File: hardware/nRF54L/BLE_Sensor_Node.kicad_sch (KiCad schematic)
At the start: 42 parts, among them U1 nRF54L05-QFXX, U2 SHTC3, U3 HDC2010, X1 32M, X2 32.768k

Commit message: nRF schematics rev: A
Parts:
- C1: footprint (none) -> Capacitor_SMD:C_0603_1608Metric; AX (none) -> 27204
- C10, C5: DigiKey (none) -> 490-12731-1-ND
- C11: DigiKey (none) -> 490-17132-1-ND
- C12, C13: DigiKey (none) -> 490-3194-1-ND
- C16: footprint (none) -> Capacitor_SMD:C_0805_2012Metric
- C7: DigiKey (none) -> 712-QLCD250Q1R5B1GV001TCT-ND
- C9: DigiKey (none) -> 490-11205-1-ND
- FB1: footprint (none) -> Inductor_SMD:L_0603_1608Metric; AX (none) -> 73236
- L1: DigiKey (none) -> 490-12065-1-ND
- L2: DigiKey (none) -> 490-15398-1-ND
- L3, L4: DigiKey (none) -> 490-15430-1-ND
- L5: value L -> 7.3n; DigiKey (none) -> 490-6844-1-ND
- L6: value L -> 6.7n; DigiKey (none) -> 490-LQW15AN6N7B00DCT-ND
- L7: now not fitted; now left out of the parts list
- R1: AX (none) -> 201001
- R2, R3: AX (none) -> 204701
- X1: value 32M -> 32MHz
- X2: value 32.768k -> 32.768kHz
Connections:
- net ANT: now also AE1.1 (Feed), L6.2, L7.1; no longer C11.1, L4.2, L5.2, L6.1
- net XL1: now reaches U1.1 (P1.00), X2.2
- net XL2: now reaches U1.2 (P1.01), X2.1
- net XC1: now reaches U1.34 (XC1), X1.1
- net XC2: now reaches U1.35 (XC2), X1.3
- new net: C11.1, L4.2, L5.2, L6.1
- no-connect marks 0 -> 26
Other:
- title: BLE Sensor Node (nRF54L varian) -> BLE Sensor Node (nRF54L variant)
- moved on the sheet: AE1, L1, X1, X2

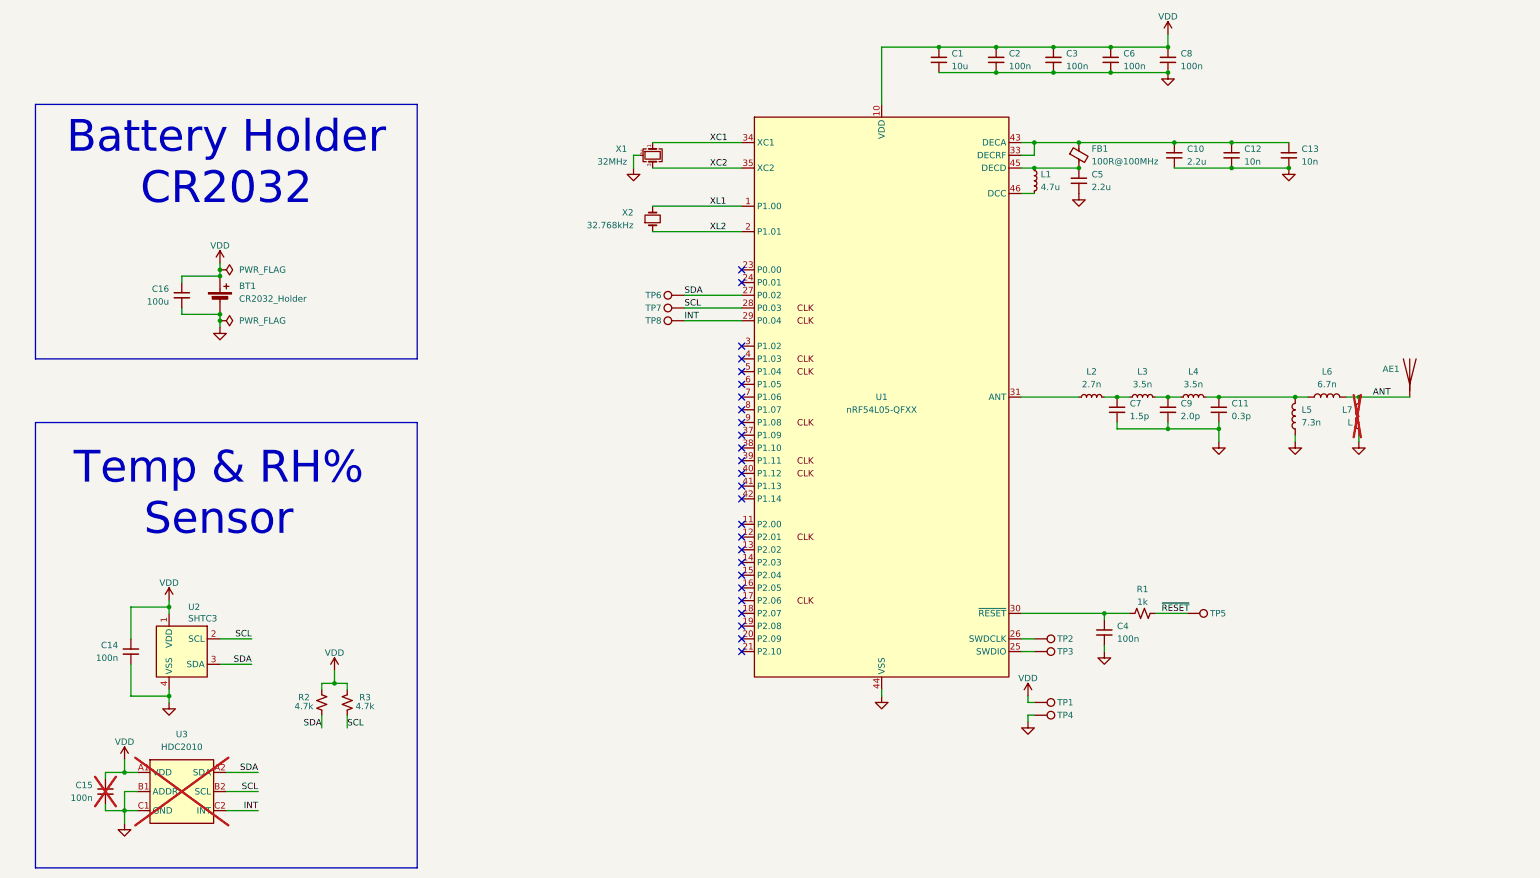
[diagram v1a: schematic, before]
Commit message: nRF54 variant routing
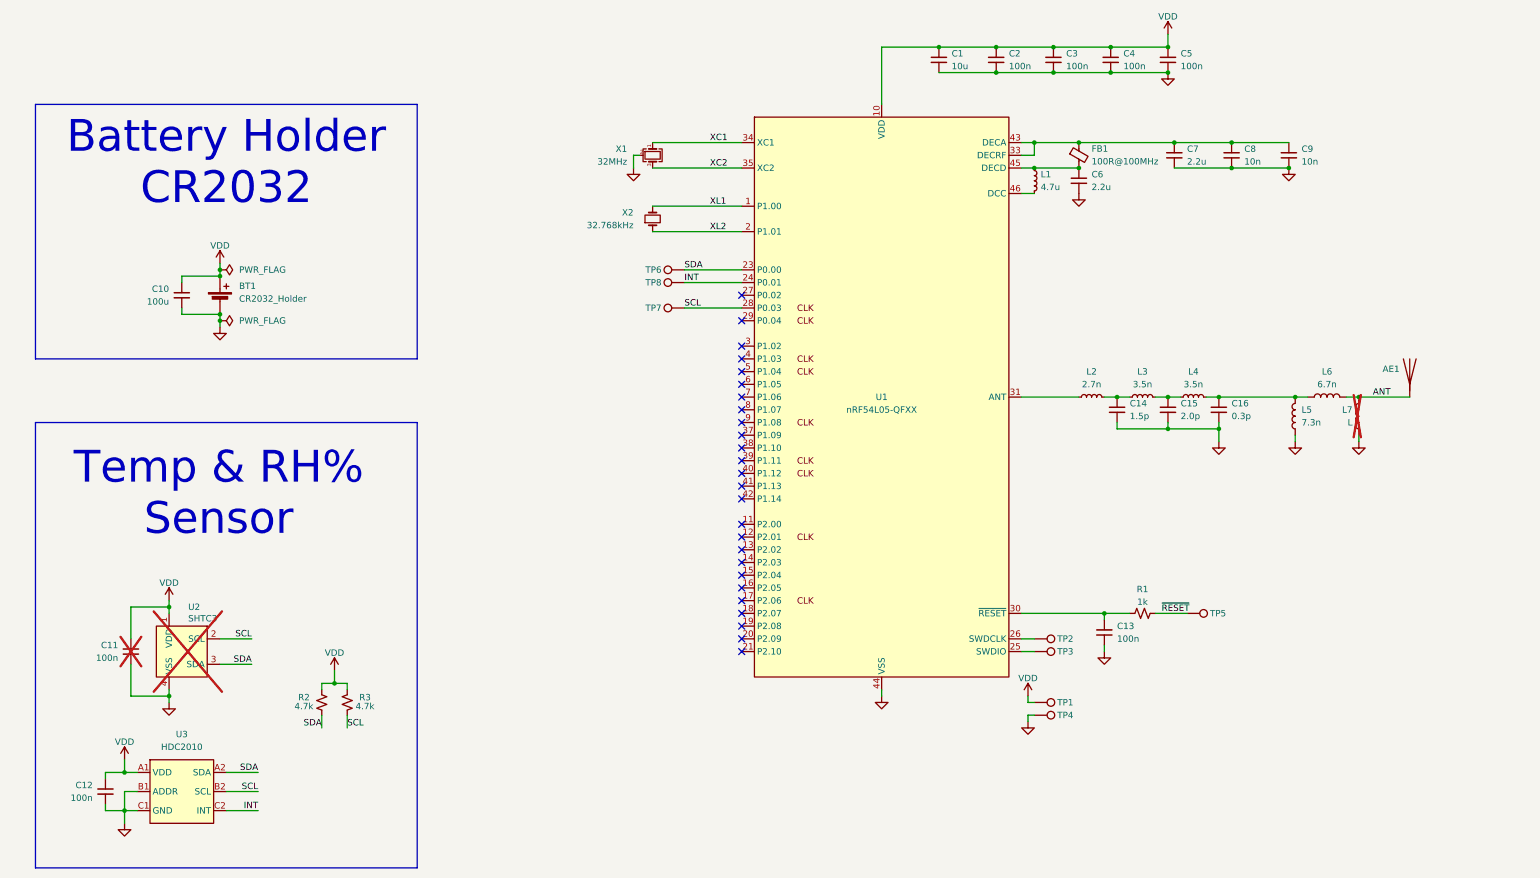
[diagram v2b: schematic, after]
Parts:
- C11: renamed from C14; now not fitted; now left out of the parts list
- C12: renamed from C15; now fitted; now in the parts list
- TP1, TP2, TP3, TP4: footprint TestPoint:TestPoint_Pad_D1.0mm -> TestPoint:TestPoint_Pad_D1.5mm
- U1: footprint Package_DFN_QFN:QFN-48-1EP_6x6mm_P0.4mm_EP4.6x4.6mm_ThermalVias -> BLE_Sensor_Node:VQFN-48-1EP_6x6mm_P0.4mm_EP4.1x4.1mm_ThermalVias
- U2: now not fitted; now left out of the parts list
- U3: now fitted; now in the parts list
- renumbered C16 to C10, C4 to C13, C7 to C14, C9 to C15, C11 to C16, C6 to C4, C8 to C5, C5 to C6, C10 to C7, C12 to C8, C13 to C9
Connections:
- net INT: now also U1.24 (P0.01); no longer U1.29 (P0.04)
- net SDA: now also U1.23 (P0.00); no longer U1.27 (P0.02)
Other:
- moved on the sheet: TP6, TP8
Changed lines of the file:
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@@
 	)
 	(no_connect
+		(at 179.07 132.08)
+	)
+	(no_connect
 		(at 179.07 165.1)
 	)
@@
 	)
 	(no_connect
-		(at 179.07 124.46)
-	)
-	(no_connect
 		(at 179.07 144.78)
 	)
@@
 	)
 	(no_connect
-		(at 179.07 121.92)
+		(at 179.07 190.5)
 	)
 	(no_connect
-		(at 179.07 190.5)
+		(at 179.07 127)
 	)
 	(no_connect
@@
 	(wire
 		(pts
-			(xy 167.64 127) (xy 179.07 127)
+			(xy 167.64 121.92) (xy 179.07 121.92)
 		)
 		(stroke
@@
 	(wire
 		(pts
-			(xy 167.64 132.08) (xy 179.07 132.08)
+			(xy 167.64 124.46) (xy 179.07 124.46)
 		)
 		(stroke
@@
 	)
 	(label "INT"
-		(at 167.64 132.08 0)
+		(at 167.64 124.46 0)
 		(effects
 			(font
@@
 	)
 	(label "SDA"
-		(at 167.64 127 0)
+		(at 167.64 121.92 0)
 		(effects
 			(font
@@
 		(dnp no)
 		(fields_autoplaced yes)
-		(property "Reference" "C10"
-			(at 267.97 97.7962 0)
+		(property "Reference" "C7"
+			(at 267.97 97.7899 0)
 			(show_name no)
 			(do_not_autoplace no)
@@
 		)
 		(property "Value" "2.2u"
-			(at 267.97 100.3362 0)
+			(at 267.97 100.3299 0)
 			(show_name no)
 			(do_not_autoplace no)
@@
 			(project "BLE_Sensor_Node"
 				(path "/3be841bb-f0fa-4f59-8a52-40b0b50ca4ae"
-					(reference "C10")
+					(reference "C7")
 					(unit 1)
 				)
@@
 		(dnp no)
 		(fields_autoplaced yes)
-		(property "Reference" "C5"
-			(at 248.92 102.8762 0)
+		(property "Reference" "C6"
+			(at 248.92 102.8699 0)
 			(show_name no)
 			(do_not_autoplace no)
@@
 		)
 		(property "Value" "2.2u"
-			(at 248.92 105.4162 0)
+			(at 248.92 105.4099 0)
 			(show_name no)
 			(do_not_autoplace no)
@@
 			(project "BLE_Sensor_Node"
 				(path "/3be841bb-f0fa-4f59-8a52-40b0b50ca4ae"
-					(reference "C5")
+					(reference "C6")
 					(unit 1)
 				)
@@
 		(dnp no)
 		(fields_autoplaced yes)
-		(property "Reference" "C11"
-			(at 276.86 148.5962 0)
+		(property "Reference" "C16"
+			(at 276.86 148.5899 0)
 			(show_name no)
 			(do_not_autoplace no)
@@
 		)
 		(property "Value" "0.3p"
-			(at 276.86 151.1362 0)
+			(at 276.86 151.1299 0)
 			(show_name no)
 			(do_not_autoplace no)
@@
 			(project "BLE_Sensor_Node"
 				(path "/3be841bb-f0fa-4f59-8a52-40b0b50ca4ae"
-					(reference "C11")
+					(reference "C16")
 					(unit 1)
 				)
@@
 		(body_style 1)
 		(exclude_from_sim no)
-		(in_bom no)
+		(in_bom yes)
 		(on_board yes)
 		(in_pos_files yes)
-		(dnp yes)
+		(dnp no)
 		(fields_autoplaced yes)
 		(property "Reference" "U3"
@@
 			)
 		)
-		(property "Footprint" "Package_DFN_QFN:QFN-48-1EP_6x6mm_P0.4mm_EP4.6x4.6mm_ThermalVias"
+		(property "Footprint" "BLE_Sensor_Node:VQFN-48-1EP_6x6mm_P0.4mm_EP4.1x4.1mm_ThermalVias"
 			(at 207.01 220.98 0)
 			(hide yes)
@@
 		(dnp no)
 		(fields_autoplaced yes)
-		(property "Reference" "C7"
-			(at 256.54 148.5962 0)
+		(property "Reference" "C14"
+			(at 256.54 148.5899 0)
 			(show_name no)
 			(do_not_autoplace no)
@@
 		)
 		(property "Value" "1.5p"
-			(at 256.54 151.1362 0)
+			(at 256.54 151.1299 0)
 			(show_name no)
 			(do_not_autoplace no)
@@
 			(project "BLE_Sensor_Node"
 				(path "/3be841bb-f0fa-4f59-8a52-40b0b50ca4ae"
-					(reference "C7")
+					(reference "C14")
 					(unit 1)
 				)
@@
 		(body_style 1)
 		(exclude_from_sim no)
-		(in_bom yes)
+		(in_bom no)
 		(on_board yes)
 		(in_pos_files yes)
-		(dnp no)
-		(property "Reference" "C14"
+		(dnp yes)
+		(property "Reference" "C11"
 			(at 54.61 196.8562 0)
 			(show_name no)
@@
 			(project "BLE_Sensor_Node"
 				(path "/3be841bb-f0fa-4f59-8a52-40b0b50ca4ae"
-					(reference "C14")
+					(reference "C11")
 					(unit 1)
 				)
@@
 			)
 		)
-		(property "Footprint" "TestPoint:TestPoint_Pad_D1.0mm"
+		(property "Footprint" "TestPoint:TestPoint_Pad_D1.5mm"
 			(at 237.49 215.9 0)
 			(hide yes)
@@
 		(dnp no)
 		(fields_autoplaced yes)
-		(property "Reference" "C12"
-			(at 279.4 97.7962 0)
+		(property "Reference" "C8"
+			(at 279.4 97.7899 0)
 			(show_name no)
 			(do_not_autoplace no)
@@
 		)
 		(property "Value" "10n"
-			(at 279.4 100.3362 0)
+			(at 279.4 100.3299 0)
 			(show_name no)
 			(do_not_autoplace no)
@@
 			(project "BLE_Sensor_Node"
 				(path "/3be841bb-f0fa-4f59-8a52-40b0b50ca4ae"
-					(reference "C12")
+					(reference "C8")
 					(unit 1)
 				)
@@
 			)
 		)
-		(property "Footprint" "TestPoint:TestPoint_Pad_D1.0mm"
+		(property "Footprint" "TestPoint:TestPoint_Pad_D1.5mm"
 			(at 237.49 200.66 0)
 			(hide yes)
@@
 		(dnp no)
 		(fields_autoplaced yes)
-		(property "Reference" "C9"
-			(at 266.7 148.5962 0)
+		(property "Reference" "C15"
+			(at 266.7 148.5899 0)
 			(show_name no)
 			(do_not_autoplace no)
@@
 		)
 		(property "Value" "2.0p"
-			(at 266.7 151.1362 0)
+			(at 266.7 151.1299 0)
 			(show_name no)
 			(do_not_autoplace no)
@@
 			(project "BLE_Sensor_Node"
 				(path "/3be841bb-f0fa-4f59-8a52-40b0b50ca4ae"
-					(reference "C9")
+					(reference "C15")
 					(unit 1)
 				)
@@
 	(symbol
 		(lib_id "Connector:TestPoint")
-		(at 167.64 127 90)
+		(at 167.64 121.92 90)
 		(unit 1)
 		(body_style 1)
@@
 		(dnp no)
 		(property "Reference" "TP6"
-			(at 163.068 127 90)
+			(at 163.068 121.92 90)
 			(show_name no)
 			(do_not_autoplace no)
@@
 		)
 		(property "Value" "TestPoint"
-			(at 162.56 125.7301 90)
+			(at 162.56 120.6501 90)
 			(hide yes)
 			(show_name no)
@@
 		)
 		(property "Footprint" "TestPoint:TestPoint_Pad_D1.0mm"
-			(at 167.64 121.92 0)
+			(at 167.64 116.84 0)
 			(hide yes)
 			(show_name no)
@@
 		)
 		(property "Datasheet" ""
-			(at 167.64 121.92 0)
+			(at 167.64 116.84 0)
 			(hide yes)
 			(show_name no)
@@
 		)
 		(property "Description" "test point"
-			(at 167.64 127 0)
+			(at 167.64 121.92 0)
 			(hide yes)
 			(show_name no)
@@
 		(dnp no)
 		(fields_autoplaced yes)
-		(property "Reference" "C8"
-			(at 266.7 78.7462 0)
+		(property "Reference" "C5"
+			(at 266.7 78.7399 0)
 			(show_name no)
 			(do_not_autoplace no)
@@
 		)
 		(property "Value" "100n"
-			(at 266.7 81.2862 0)
+			(at 266.7 81.2799 0)
 			(show_name no)
 			(do_not_autoplace no)
@@
 			(project "BLE_Sensor_Node"
 				(path "/3be841bb-f0fa-4f59-8a52-40b0b50ca4ae"
-					(reference "C8")
+					(reference "C5")
 					(unit 1)
 				)
@@
 		(body_style 1)
 		(exclude_from_sim no)
-		(in_bom no)
+		(in_bom yes)
 		(on_board yes)
 		(in_pos_files yes)
-		(dnp yes)
-		(property "Reference" "C15"
+		(dnp no)
+		(property "Reference" "C12"
 			(at 49.53 224.7962 0)
 			(show_name no)
@@
 			(project "BLE_Sensor_Node"
 				(path "/3be841bb-f0fa-4f59-8a52-40b0b50ca4ae"
-					(reference "C15")
+					(reference "C12")
 					(unit 1)
 				)
@@
 			)
 		)
-		(property "Footprint" "TestPoint:TestPoint_Pad_D1.0mm"
+		(property "Footprint" "TestPoint:TestPoint_Pad_D1.5mm"
 			(at 237.49 213.36 0)
 			(hide yes)
@@
 		(body_style 1)
 		(exclude_from_sim no)
-		(in_bom yes)
+		(in_bom no)
 		(on_board yes)
 		(in_pos_files yes)
-		(dnp no)
+		(dnp yes)
 		(property "Reference" "U2"
 			(at 68.58 189.23 0)
@@
 		(dnp no)
 		(fields_autoplaced yes)
-		(property "Reference" "C4"
-			(at 254 193.0462 0)
+		(property "Reference" "C13"
+			(at 254 193.0399 0)
 			(show_name no)
 			(do_not_autoplace no)
@@
 		)
 		(property "Value" "100n"
-			(at 254 195.5862 0)
+			(at 254 195.5799 0)
 			(show_name no)
 			(do_not_autoplace no)
@@
 			(project "BLE_Sensor_Node"
 				(path "/3be841bb-f0fa-4f59-8a52-40b0b50ca4ae"
-					(reference "C4")
+					(reference "C13")
 					(unit 1)
 				)
@@
 	(symbol
 		(lib_id "Connector:TestPoint")
-		(at 167.64 132.08 90)
+		(at 167.64 124.46 90)
 		(unit 1)
 		(body_style 1)
@@
 		(dnp no)
 		(property "Reference" "TP8"
-			(at 163.068 132.08 90)
+			(at 163.068 124.46 90)
 			(show_name no)
 			(do_not_autoplace no)
@@
 		)
 		(property "Value" "TestPoint"
-			(at 162.56 130.8101 90)
+			(at 162.56 123.1901 90)
 			(hide yes)
 			(show_name no)
@@
 		)
 		(property "Footprint" "TestPoint:TestPoint_Pad_D1.0mm"
-			(at 167.64 127 0)
+			(at 167.64 119.38 0)
 			(hide yes)
 			(show_name no)
@@
 		)
 		(property "Datasheet" ""
-			(at 167.64 127 0)
+			(at 167.64 119.38 0)
 			(hide yes)
 			(show_name no)
@@
 		)
 		(property "Description" "test point"
-			(at 167.64 132.08 0)
+			(at 167.64 124.46 0)
 			(hide yes)
 			(show_name no)
@@
 		(dnp no)
 		(fields_autoplaced yes)
-		(property "Reference" "C13"
-			(at 290.83 97.7962 0)
+		(property "Reference" "C9"
+			(at 290.83 97.7899 0)
 			(show_name no)
 			(do_not_autoplace no)
@@
 		)
 		(property "Value" "10n"
-			(at 290.83 100.3362 0)
+			(at 290.83 100.3299 0)
 			(show_name no)
 			(do_not_autoplace no)
@@
 			(project "BLE_Sensor_Node"
 				(path "/3be841bb-f0fa-4f59-8a52-40b0b50ca4ae"
-					(reference "C13")
+					(reference "C9")
 					(unit 1)
 				)
@@
 			)
 		)
-		(property "Footprint" "TestPoint:TestPoint_Pad_D1.0mm"
+		(property "Footprint" "TestPoint:TestPoint_Pad_D1.5mm"
 			(at 237.49 203.2 0)
 			(hide yes)
@@
 		(dnp no)
 		(fields_autoplaced yes)
-		(property "Reference" "C6"
-			(at 255.27 78.7462 0)
+		(property "Reference" "C4"
+			(at 255.27 78.7399 0)
 			(show_name no)
 			(do_not_autoplace no)
@@
 		)
 		(property "Value" "100n"
-			(at 255.27 81.2862 0)
+			(at 255.27 81.2799 0)
 			(show_name no)
 			(do_not_autoplace no)
@@
 			(project "BLE_Sensor_Node"
 				(path "/3be841bb-f0fa-4f59-8a52-40b0b50ca4ae"
-					(reference "C6")
+					(reference "C4")
 					(unit 1)
 				)
@@
 		(in_pos_files yes)
 		(dnp no)
-		(property "Reference" "C16"
+		(property "Reference" "C10"
 			(at 64.77 125.7362 0)
 			(show_name no)
@@
 			(project "BLE_Sensor_Node"
 				(path "/3be841bb-f0fa-4f59-8a52-40b0b50ca4ae"
-					(reference "C16")
+					(reference "C10")
 					(unit 1)
 				)

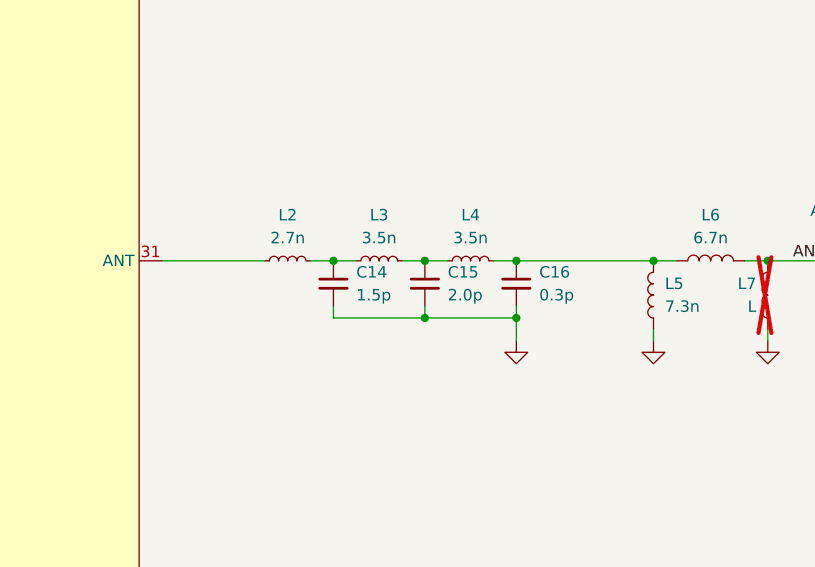
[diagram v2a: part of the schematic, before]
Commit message: Added optional U.FL connector and stiching vias
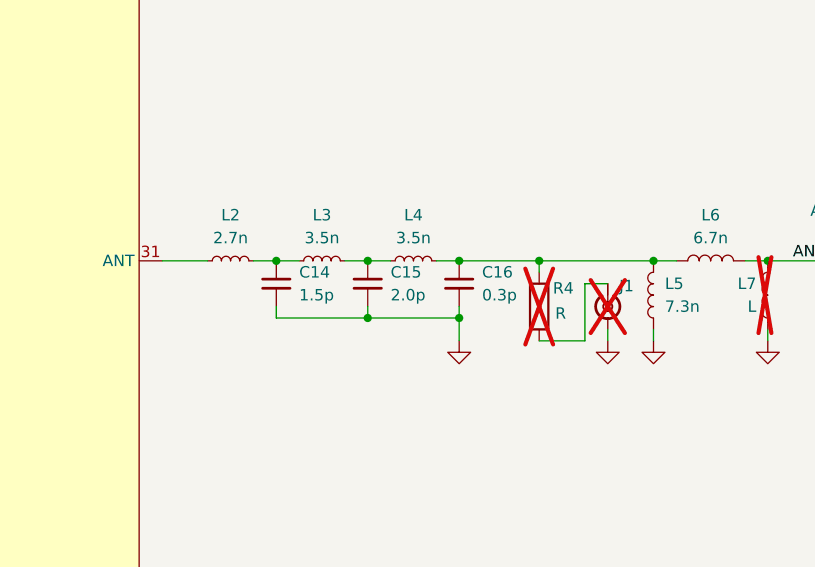
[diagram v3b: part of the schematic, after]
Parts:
- added J1: Conn_Coaxial_Small, Connector_Coaxial:U.FL_Hirose_U.FL-R-SMT-1_Vertical, symbol Connector:Conn_Coaxial_Small
- added R4: R, Resistor_SMD:R_0201_0603Metric, symbol Device:R
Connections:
- net GND: now also J1.2 (Ext)
- net at C16.1, L4.2, L5.2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: now also R4.1
- new net: J1.1 (In), R4.2
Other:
- moved on the sheet: C14, C15, C16, L2, L3, L4

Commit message: First Rev of the nRF variant
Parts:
- TP1, TP2, TP3, TP4, TP5, TP6, TP7, TP8: now left out of the parts list
- U2: now in the parts list
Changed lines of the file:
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@@
 		(body_style 1)
 		(exclude_from_sim no)
-		(in_bom yes)
+		(in_bom no)
 		(on_board yes)
 		(in_pos_files yes)
@@
 		(body_style 1)
 		(exclude_from_sim no)
-		(in_bom yes)
+		(in_bom no)
 		(on_board yes)
 		(in_pos_files yes)
@@
 			)
 		)
-		(property "Sim.Device" "V"
-			(at 74.93 128.27 0)
-			(hide yes)
-			(show_name no)
-			(do_not_autoplace no)
-			(effects
-				(font
-					(size 1.27 1.27)
-				)
-			)
-		)
-		(property "Sim.Type" "DC"
-			(at 74.93 128.27 0)
-			(hide yes)
-			(show_name no)
-			(do_not_autoplace no)
-			(effects
-				(font
-					(size 1.27 1.27)
-				)
-			)
-		)
-		(property "Sim.Pins" "1=+ 2=-"
-			(at 74.93 128.27 0)
-			(hide yes)
-			(show_name no)
-			(do_not_autoplace no)
-			(effects
-				(font
-					(size 1.27 1.27)
-				)
-			)
-		)
 		(pin "2"
 		)
@@
 		(body_style 1)
 		(exclude_from_sim no)
-		(in_bom yes)
+		(in_bom no)
 		(on_board yes)
 		(in_pos_files yes)
@@
 		(body_style 1)
 		(exclude_from_sim no)
-		(in_bom yes)
+		(in_bom no)
 		(on_board yes)
 		(in_pos_files yes)
@@
 		(body_style 1)
 		(exclude_from_sim no)
-		(in_bom yes)
+		(in_bom no)
 		(on_board yes)
 		(in_pos_files yes)
@@
 		(body_style 1)
 		(exclude_from_sim no)
-		(in_bom yes)
+		(in_bom no)
 		(on_board yes)
 		(in_pos_files yes)
@@
 		(body_style 1)
 		(exclude_from_sim no)
-		(in_bom no)
+		(in_bom yes)
 		(on_board yes)
 		(in_pos_files yes)
@@
 		(body_style 1)
 		(exclude_from_sim no)
-		(in_bom yes)
+		(in_bom no)
 		(on_board yes)
 		(in_pos_files yes)
@@
 		(body_style 1)
 		(exclude_from_sim no)
-		(in_bom yes)
+		(in_bom no)
 		(on_board yes)
 		(in_pos_files yes)
